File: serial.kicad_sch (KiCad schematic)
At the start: 58 parts, among them IC3 ILD217T, U16 SP3485EN, U3 ADM2483xRW, U4 ADuM1201AR, U6 ADuM1201AR, U8 SP3485EN, X2 Conn_S1

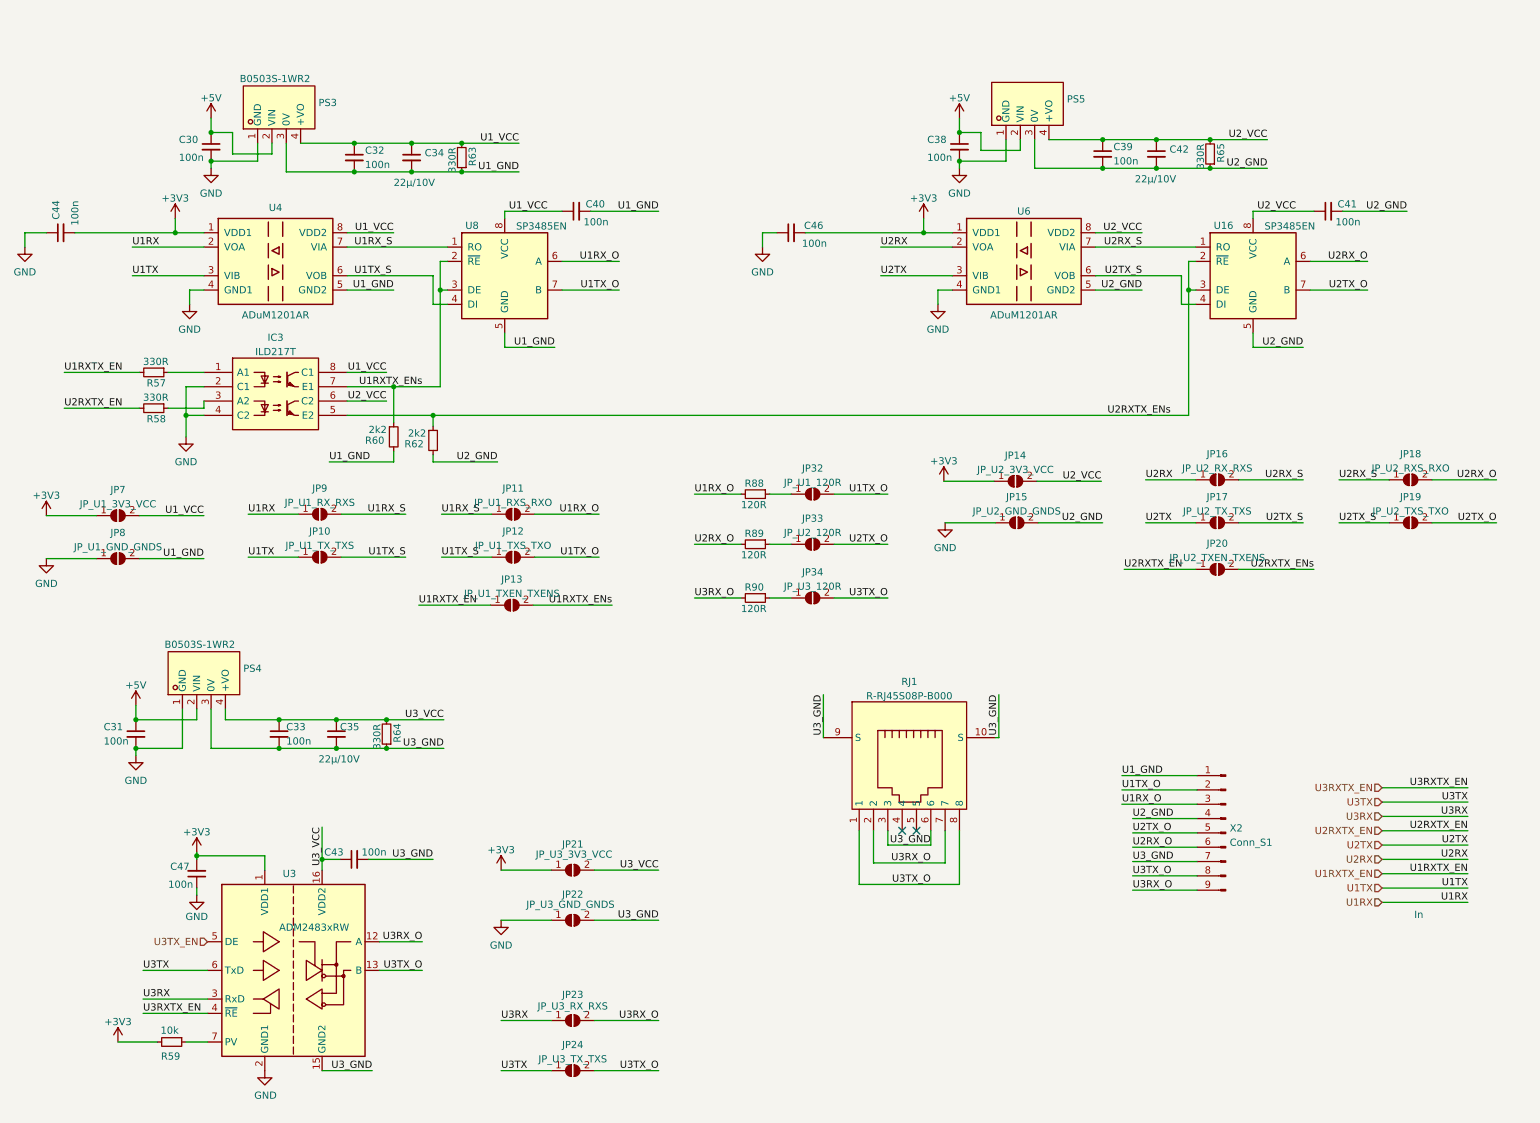
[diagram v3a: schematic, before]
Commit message: Improvements added (Ref 2.4.1)
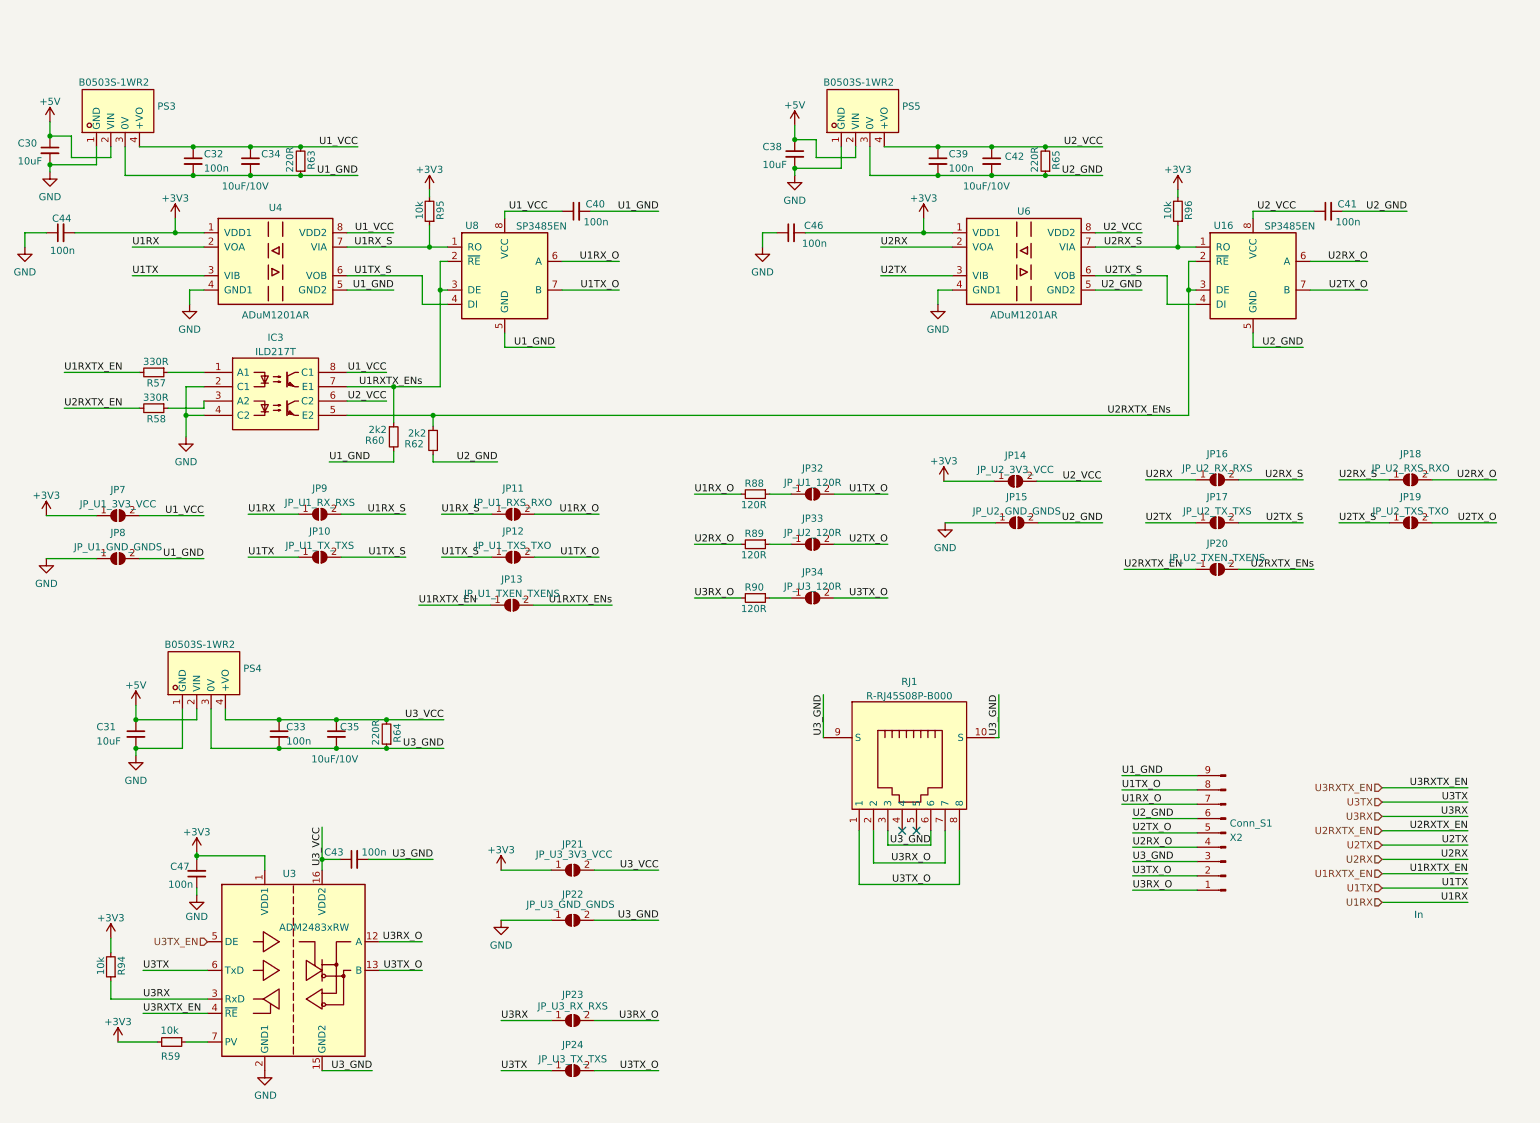
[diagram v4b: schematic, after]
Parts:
- added R94, R95, R96: 10k, Resistor_SMD:R_0603_1608Metric, symbol Device:R_Small
- C30, C31, C38: value 100n -> 10uF
- C34, C35, C42: value 22µ/10V -> 10uF/10V
- PS5: value (none) -> B0503S-1WR2; footprint (none) -> lcsc:PWRM-TH_DEXU_BXXXXS-1WR2
- R63, R64, R65: value 330R -> 220R; footprint Resistor_SMD:R_0603_1608Metric -> Resistor_SMD:R_0805_2012Metric
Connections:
- net +3V3: now also R94.2, R95.2, R96.2
- net U1RX_O: now also X2.7 (Pin_7); no longer X2.3 (Pin_3)
- net U1RX_S: now also R95.1
- net U1TX_O: now also X2.8 (Pin_8); no longer X2.2 (Pin_2)
- net U1_GND: now also X2.9 (Pin_9); no longer X2.1 (Pin_1)
- net U2RX_O: now also X2.4 (Pin_4); no longer X2.6 (Pin_6)
- net U2RX_S: now also R96.1
- net U2_GND: now also X2.6 (Pin_6); no longer X2.4 (Pin_4)
- net U3RX: now also R94.1
- net U3RX_O: now also X2.1 (Pin_1); no longer X2.9 (Pin_9)
- net U3TX_O: now also X2.2 (Pin_2); no longer X2.8 (Pin_8)
- net U3_GND: now also X2.3 (Pin_3); no longer X2.7 (Pin_7)
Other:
- moved on the sheet: C30, C32, C34, C38, C39, C42, PS3, PS5, R63, R65, X2

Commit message: RX Pullups von U1+U2 geändert
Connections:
- net +3V3: no longer R95.2, R96.2
- net U1_VCC: now also R95.2
- net U2_VCC: now also R96.2
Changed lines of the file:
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@@
   (title_block
     (title "BSC")
-    (date "2023-06-25")
+    (date "2024-03-29")
     (rev "2.4.1")
   )
@@
     (stroke (width 0) (type default))
   )
-  (wire (pts (xy 222.25 33.655) (xy 222.25 34.925))
+  (wire (pts (xy 222.25 27.305) (xy 222.25 34.925))
     (stroke (width 0) (type default))
   )
@@
     (stroke (width 0) (type default))
   )
-  (wire (pts (xy 89.535 33.655) (xy 89.535 34.925))
+  (wire (pts (xy 89.535 27.94) (xy 89.535 34.925))
     (stroke (width 0) (type default))
   )
@@
     (effects (font (size 1.27 1.27)) (justify left bottom))
   )
+  (label "U2_VCC" (at 222.25 27.305 270) (fields_autoplaced)
+    (effects (font (size 1.27 1.27)) (justify right bottom))
+  )
   (label "U1RX_O" (at 136.525 87.63 0) (fields_autoplaced)
     (effects (font (size 1.27 1.27)) (justify left bottom))
@@
   )
   (label "U2RX" (at 273.685 152.4 180) (fields_autoplaced)
+    (effects (font (size 1.27 1.27)) (justify right bottom))
+  )
+  (label "U1_VCC" (at 89.535 27.94 270) (fields_autoplaced)
     (effects (font (size 1.27 1.27)) (justify right bottom))
   )
@@
     )
   )
-  (symbol (lib_id "power:+3V3") (at 89.535 33.655 0) (unit 1)
-    (in_bom yes) (on_board yes) (dnp no)
-    (property "Reference" "#PWR046" (at 89.535 37.465 0)
-      (effects (font (size 1.27 1.27)) hide)
-    )
-    (property "Value" "+3V3" (at 89.535 30.0792 0)
-      (effects (font (size 1.27 1.27)))
-    )
-    (property "Footprint" "" (at 89.535 33.655 0)
-      (effects (font (size 1.27 1.27)) hide)
-    )
-    (property "Datasheet" "" (at 89.535 33.655 0)
-      (effects (font (size 1.27 1.27)) hide)
-    )
-    (pin "1")
-    (instances
-      (project "bsc"
-        (path "/e63e39d7-6ac0-4ffd-8aa3-1841a4541b55/59c4824a-ae1a-4fd0-b4ff-eae76325ec0c"
-          (reference "#PWR046") (unit 1)
-        )
-      )
-    )
-  )
   (symbol (lib_id "power:GND") (at 60.325 189.865 0) (unit 1)
     (in_bom yes) (on_board yes) (dnp no)
@@
         )
       )
-    )
-  )
-  (symbol (lib_id "power:+3V3") (at 222.25 33.655 0) (unit 1)
-    (in_bom yes) (on_board yes) (dnp no)
-    (property "Reference" "#PWR056" (at 222.25 37.465 0)
-      (effects (font (size 1.27 1.27)) hide)
-    )
-    (property "Value" "+3V3" (at 222.25 30.0792 0)
-      (effects (font (size 1.27 1.27)))
-    )
-    (property "Footprint" "" (at 222.25 33.655 0)
-      (effects (font (size 1.27 1.27)) hide)
-    )
-    (property "Datasheet" "" (at 222.25 33.655 0)
-      (effects (font (size 1.27 1.27)) hide)
-    )
-    (pin "1")
-    (instances
-      (project "bsc"
-        (path "/e63e39d7-6ac0-4ffd-8aa3-1841a4541b55/59c4824a-ae1a-4fd0-b4ff-eae76325ec0c"
-          (reference "#PWR056") (unit 1)
-        )
-      )
